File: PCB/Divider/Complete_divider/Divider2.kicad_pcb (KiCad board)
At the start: 2 copper layers, 98 x 48 mm, 56 parts, among them J31 Electr., J58 Electr.

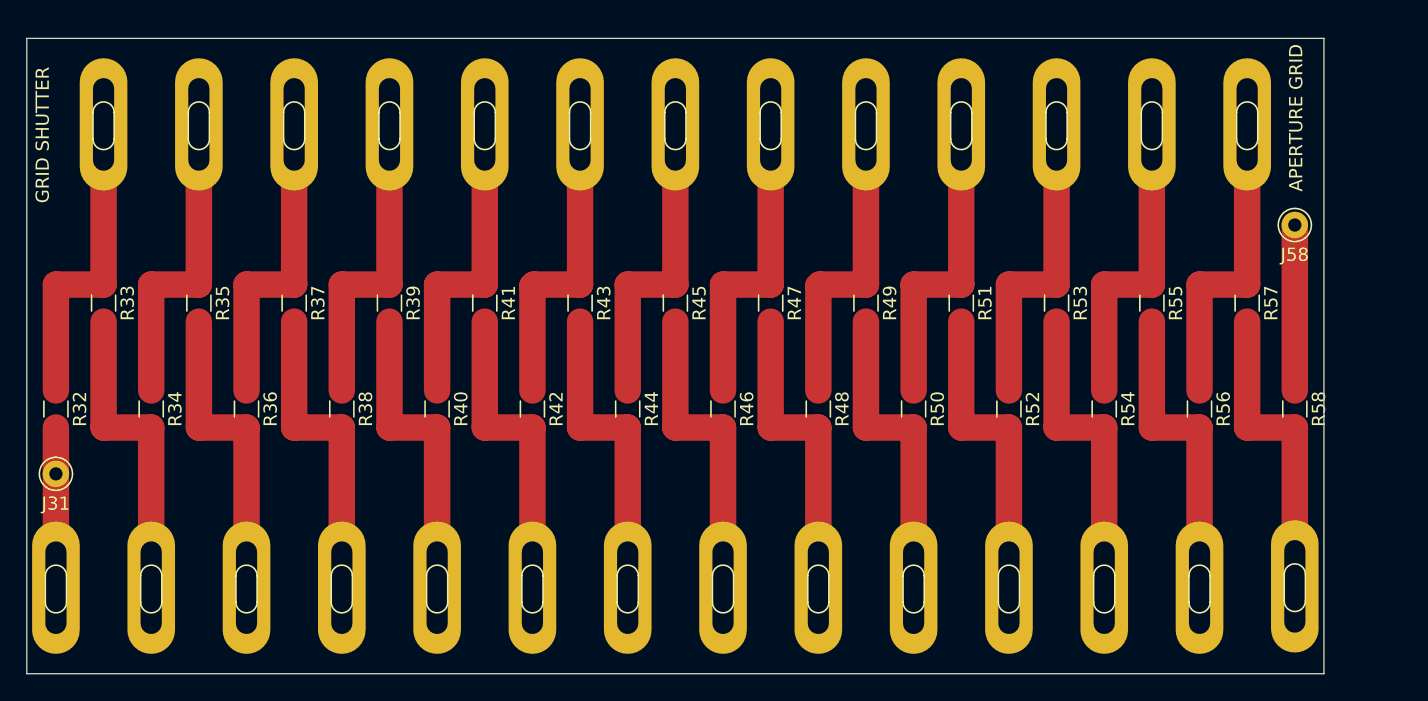
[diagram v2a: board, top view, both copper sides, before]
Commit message: Divider finished with test points
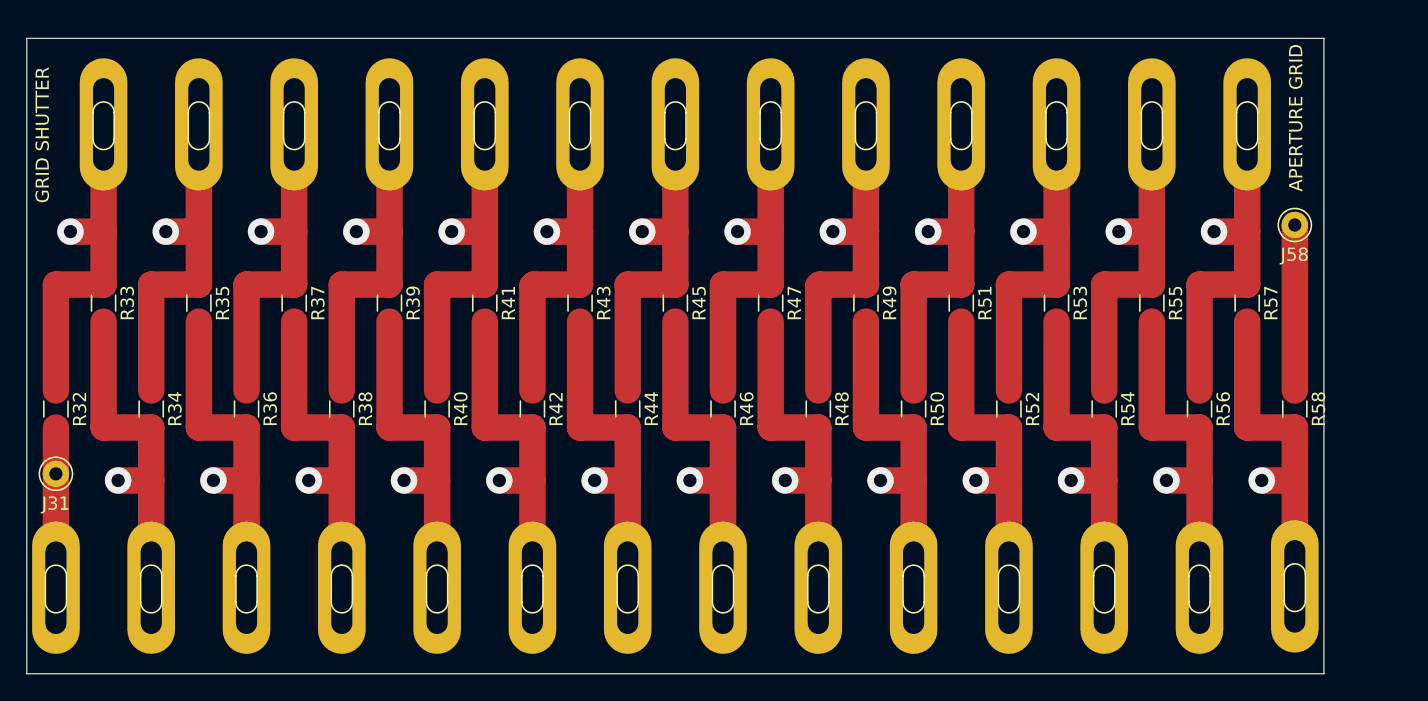
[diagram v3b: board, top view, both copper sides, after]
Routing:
- net Net-(E57-Pad1): track 23.6 -> 26.1 mm, vias 0 -> 1
- net Net-(E56-Pad1): track 23.7 -> 26.2 mm, vias 0 -> 1
- net Net-(E55-Pad1): track 23.7 -> 26.2 mm, vias 0 -> 1
- net Net-(E54-Pad1): track 23.7 -> 26.2 mm, vias 0 -> 1
- net Net-(E53-Pad1): track 23.7 -> 26.2 mm, vias 0 -> 1
- net Net-(E52-Pad1): track 23.7 -> 26.2 mm, vias 0 -> 1
- net Net-(E51-Pad1): track 23.7 -> 26.2 mm, vias 0 -> 1
- net Net-(E50-Pad1): track 23.7 -> 26.2 mm, vias 0 -> 1
- net Net-(E49-Pad1): track 23.7 -> 26.2 mm, vias 0 -> 1
- net Net-(E48-Pad1): track 23.6 -> 26.1 mm, vias 0 -> 1
- net Net-(E47-Pad1): track 23.7 -> 26.2 mm, vias 0 -> 1
- net Net-(E46-Pad1): track 23.7 -> 26.2 mm, vias 0 -> 1
- net Net-(E45-Pad1): track 23.7 -> 26.2 mm, vias 0 -> 1
- net Net-(E44-Pad1): track 23.7 -> 26.2 mm, vias 0 -> 1
- net Net-(E43-Pad1): track 23.7 -> 26.2 mm, vias 0 -> 1
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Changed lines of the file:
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@@
     (thickness 1.6)
     (drawings 16)
-    (tracks 83)
+    (tracks 162)
     (zones 0)
     (modules 56)
@@
     (via_min_size 0.4)
     (via_min_drill 0.3)
+    (user_via 2 1)
     (uvia_size 0.3)
     (uvia_drill 0.1)
@@
   (segment (start 99.6 109.2) (end 99.6 100.6) (width 2) (layer F.Cu) (net 2))
   (segment (start 99.6 100.6) (end 99.6 97.1) (width 2) (layer F.Cu) (net 2))
-  (segment (start 103.2 74.2) (end 103.2 86.3) (width 2) (layer F.Cu) (net 3))
   (segment (start 99.6 94.3) (end 99.6 86.3) (width 2) (layer F.Cu) (net 3))
   (segment (start 99.6 86.3) (end 103.2 86.3) (width 2) (layer F.Cu) (net 3))
+  (segment (start 103.2 74.2) (end 103.2 82.3) (width 2) (layer F.Cu) (net 3))
+  (segment (start 103.2 82.3) (end 100.7 82.3) (width 2) (layer F.Cu) (net 3))
+  (segment (start 103.2 82.3) (end 103.2 86.3) (width 2) (layer F.Cu) (net 3))
+  (segment (start 100.7 82.3) (end 100.7 82.3) (width 2) (layer F.Cu) (net 3))
+  (via (at 100.7 82.3) (size 2) (drill 1) (layers F.Cu B.Cu) (net 3))
+  (segment (start 107.9 82.3) (end 107.9 82.3) (width 2) (layer F.Cu) (net 5))
+  (segment (start 115.1 82.3) (end 115.1 82.3) (width 2) (layer F.Cu) (net 7))
+  (segment (start 122.3 82.3) (end 122.3 82.3) (width 2) (layer F.Cu) (net 9))
+  (segment (start 129.5 82.3) (end 129.5 82.3) (width 2) (layer F.Cu) (net 11))
+  (segment (start 136.7 82.3) (end 136.7 82.3) (width 2) (layer F.Cu) (net 13))
+  (segment (start 143.9 82.3) (end 143.9 82.3) (width 2) (layer F.Cu) (net 15))
+  (segment (start 151.1 82.3) (end 151.1 82.3) (width 2) (layer F.Cu) (net 17))
+  (segment (start 158.3 82.3) (end 158.3 82.3) (width 2) (layer F.Cu) (net 19))
+  (segment (start 165.5 82.3) (end 165.5 82.3) (width 2) (layer F.Cu) (net 21))
+  (segment (start 172.7 82.3) (end 172.7 82.3) (width 2) (layer F.Cu) (net 23))
+  (segment (start 179.9 82.3) (end 179.9 82.3) (width 2) (layer F.Cu) (net 25))
+  (segment (start 187.1 82.3) (end 187.1 82.3) (width 2) (layer F.Cu) (net 27))
+  (segment (start 104.3 101.1) (end 104.3 101.1) (width 2) (layer F.Cu) (net 4))
+  (segment (start 111.5 101.1) (end 111.5 101.1) (width 2) (layer F.Cu) (net 6))
+  (segment (start 118.7 101.1) (end 118.7 101.1) (width 2) (layer F.Cu) (net 8))
+  (segment (start 125.9 101.1) (end 125.9 101.1) (width 2) (layer F.Cu) (net 10))
+  (segment (start 133.1 101.1) (end 133.1 101.1) (width 2) (layer F.Cu) (net 12))
+  (segment (start 140.3 101.1) (end 140.3 101.1) (width 2) (layer F.Cu) (net 14))
+  (segment (start 147.5 101.1) (end 147.5 101.1) (width 2) (layer F.Cu) (net 16))
+  (segment (start 154.7 101.1) (end 154.7 101.1) (width 2) (layer F.Cu) (net 18))
+  (segment (start 161.9 101.1) (end 161.9 101.1) (width 2) (layer F.Cu) (net 20))
+  (segment (start 169.1 101.1) (end 169.1 101.1) (width 2) (layer F.Cu) (net 22))
+  (segment (start 176.3 101.1) (end 176.3 101.1) (width 2) (layer F.Cu) (net 24))
+  (segment (start 183.5 101.1) (end 183.5 101.1) (width 2) (layer F.Cu) (net 26))
+  (segment (start 190.7 101.1) (end 190.7 101.1) (width 2) (layer F.Cu) (net 28))
+  (via (at 107.9 82.3) (size 2) (drill 1) (layers F.Cu B.Cu) (net 5))
+  (via (at 115.1 82.3) (size 2) (drill 1) (layers F.Cu B.Cu) (net 7))
+  (via (at 122.3 82.3) (size 2) (drill 1) (layers F.Cu B.Cu) (net 9))
+  (via (at 129.5 82.3) (size 2) (drill 1) (layers F.Cu B.Cu) (net 11))
+  (via (at 136.7 82.3) (size 2) (drill 1) (layers F.Cu B.Cu) (net 13))
+  (via (at 143.9 82.3) (size 2) (drill 1) (layers F.Cu B.Cu) (net 15))
+  (via (at 151.1 82.3) (size 2) (drill 1) (layers F.Cu B.Cu) (net 17))
+  (via (at 158.3 82.3) (size 2) (drill 1) (layers F.Cu B.Cu) (net 19))
+  (via (at 165.5 82.3) (size 2) (drill 1) (layers F.Cu B.Cu) (net 21))
+  (via (at 172.7 82.3) (size 2) (drill 1) (layers F.Cu B.Cu) (net 23))
+  (via (at 179.9 82.3) (size 2) (drill 1) (layers F.Cu B.Cu) (net 25))
+  (via (at 187.1 82.3) (size 2) (drill 1) (layers F.Cu B.Cu) (net 27))
+  (via (at 104.3 101.1) (size 2) (drill 1) (layers F.Cu B.Cu) (net 4))
+  (via (at 111.5 101.1) (size 2) (drill 1) (layers F.Cu B.Cu) (net 6))
+  (via (at 118.7 101.1) (size 2) (drill 1) (layers F.Cu B.Cu) (net 8))
+  (via (at 125.9 101.1) (size 2) (drill 1) (layers F.Cu B.Cu) (net 10))
+  (via (at 133.1 101.1) (size 2) (drill 1) (layers F.Cu B.Cu) (net 12))
+  (via (at 140.3 101.1) (size 2) (drill 1) (layers F.Cu B.Cu) (net 14))
+  (via (at 147.5 101.1) (size 2) (drill 1) (layers F.Cu B.Cu) (net 16))
+  (via (at 154.7 101.1) (size 2) (drill 1) (layers F.Cu B.Cu) (net 18))
+  (via (at 161.9 101.1) (size 2) (drill 1) (layers F.Cu B.Cu) (net 20))
+  (via (at 169.1 101.1) (size 2) (drill 1) (layers F.Cu B.Cu) (net 22))
+  (via (at 176.3 101.1) (size 2) (drill 1) (layers F.Cu B.Cu) (net 24))
+  (via (at 183.5 101.1) (size 2) (drill 1) (layers F.Cu B.Cu) (net 26))
+  (via (at 190.7 101.1) (size 2) (drill 1) (layers F.Cu B.Cu) (net 28))
+  (segment (start 110.4 82.3) (end 107.9 82.3) (width 2) (layer F.Cu) (net 5))
+  (segment (start 117.6 82.3) (end 115.1 82.3) (width 2) (layer F.Cu) (net 7))
+  (segment (start 124.8 82.3) (end 122.3 82.3) (width 2) (layer F.Cu) (net 9))
+  (segment (start 132 82.3) (end 129.5 82.3) (width 2) (layer F.Cu) (net 11))
+  (segment (start 139.2 82.3) (end 136.7 82.3) (width 2) (layer F.Cu) (net 13))
+  (segment (start 146.4 82.3) (end 143.9 82.3) (width 2) (layer F.Cu) (net 15))
+  (segment (start 153.6 82.3) (end 151.1 82.3) (width 2) (layer F.Cu) (net 17))
+  (segment (start 160.8 82.3) (end 158.3 82.3) (width 2) (layer F.Cu) (net 19))
+  (segment (start 168 82.3) (end 165.5 82.3) (width 2) (layer F.Cu) (net 21))
+  (segment (start 175.2 82.3) (end 172.7 82.3) (width 2) (layer F.Cu) (net 23))
+  (segment (start 182.4 82.3) (end 179.9 82.3) (width 2) (layer F.Cu) (net 25))
+  (segment (start 189.6 82.3) (end 187.1 82.3) (width 2) (layer F.Cu) (net 27))
+  (segment (start 106.8 101.1) (end 104.3 101.1) (width 2) (layer F.Cu) (net 4))
+  (segment (start 114 101.1) (end 111.5 101.1) (width 2) (layer F.Cu) (net 6))
+  (segment (start 121.2 101.1) (end 118.7 101.1) (width 2) (layer F.Cu) (net 8))
+  (segment (start 128.4 101.1) (end 125.9 101.1) (width 2) (layer F.Cu) (net 10))
+  (segment (start 135.6 101.1) (end 133.1 101.1) (width 2) (layer F.Cu) (net 12))
+  (segment (start 142.8 101.1) (end 140.3 101.1) (width 2) (layer F.Cu) (net 14))
+  (segment (start 150 101.1) (end 147.5 101.1) (width 2) (layer F.Cu) (net 16))
+  (segment (start 157.2 101.1) (end 154.7 101.1) (width 2) (layer F.Cu) (net 18))
+  (segment (start 164.4 101.1) (end 161.9 101.1) (width 2) (layer F.Cu) (net 20))
+  (segment (start 171.6 101.1) (end 169.1 101.1) (width 2) (layer F.Cu) (net 22))
+  (segment (start 178.8 101.1) (end 176.3 101.1) (width 2) (layer F.Cu) (net 24))
+  (segment (start 186 101.1) (end 183.5 101.1) (width 2) (layer F.Cu) (net 26))
+  (segment (start 193.2 101.1) (end 190.7 101.1) (width 2) (layer F.Cu) (net 28))
   (segment (start 103.2 89.1) (end 103.2 97.1) (width 2) (layer F.Cu) (net 4))
   (segment (start 103.2 97.1) (end 106.8 97.1) (width 2) (layer F.Cu) (net 4))

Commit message: Most parts completed
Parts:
- renumbered J58 to E58, R32 to R31, R33 to R32, R34 to R33, R35 to R34, R36 to R35, R37 to R36, R38 to R37, R39 to R38, R40 to R39, R41 to R40, R42 to R41, R43 to R42, R44 to R43, R45 to R44, R46 to R45, R47 to R46, R48 to R47, R49 to R48, R50 to R49, R51 to R50, R52 to R51, R53 to R52, R54 to R53, R55 to R54, R56 to R55, R57 to R56, R58 to R57

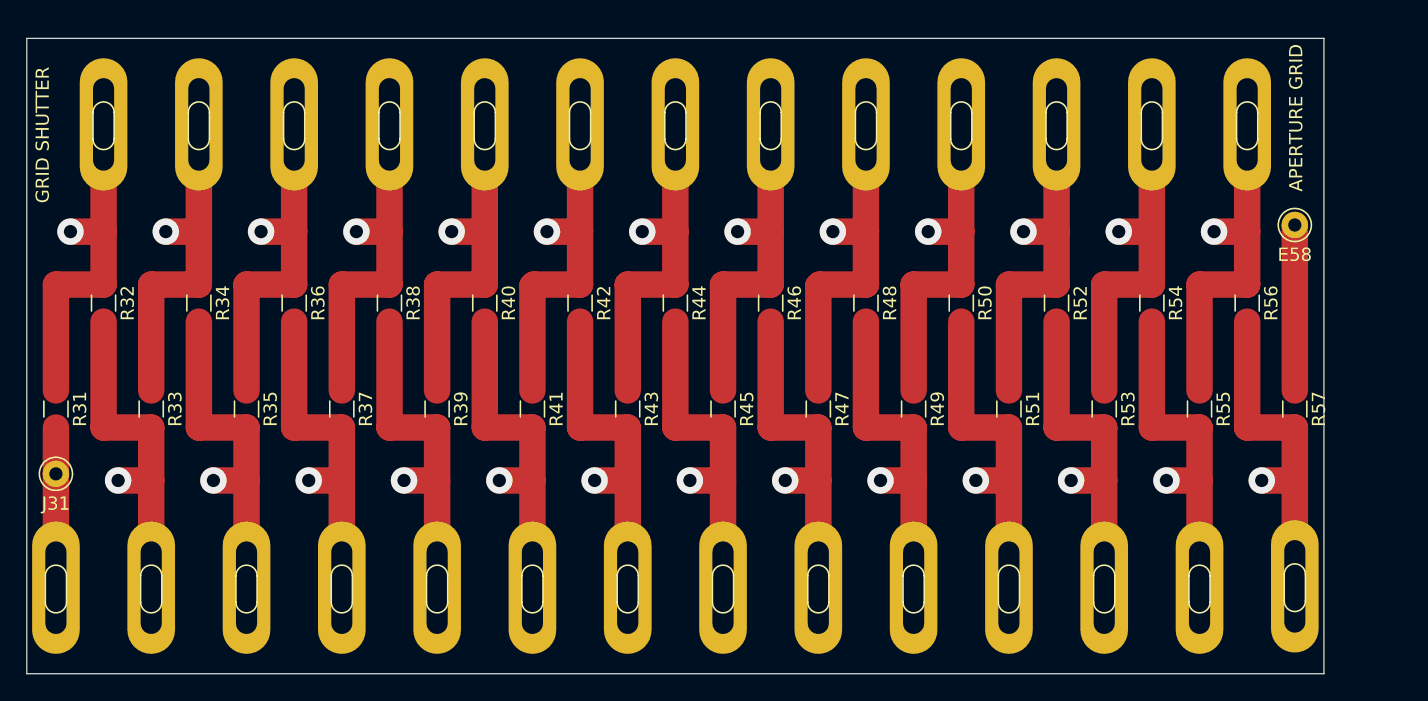
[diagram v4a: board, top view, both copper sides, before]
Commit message: Updates of dividers 1 & 2
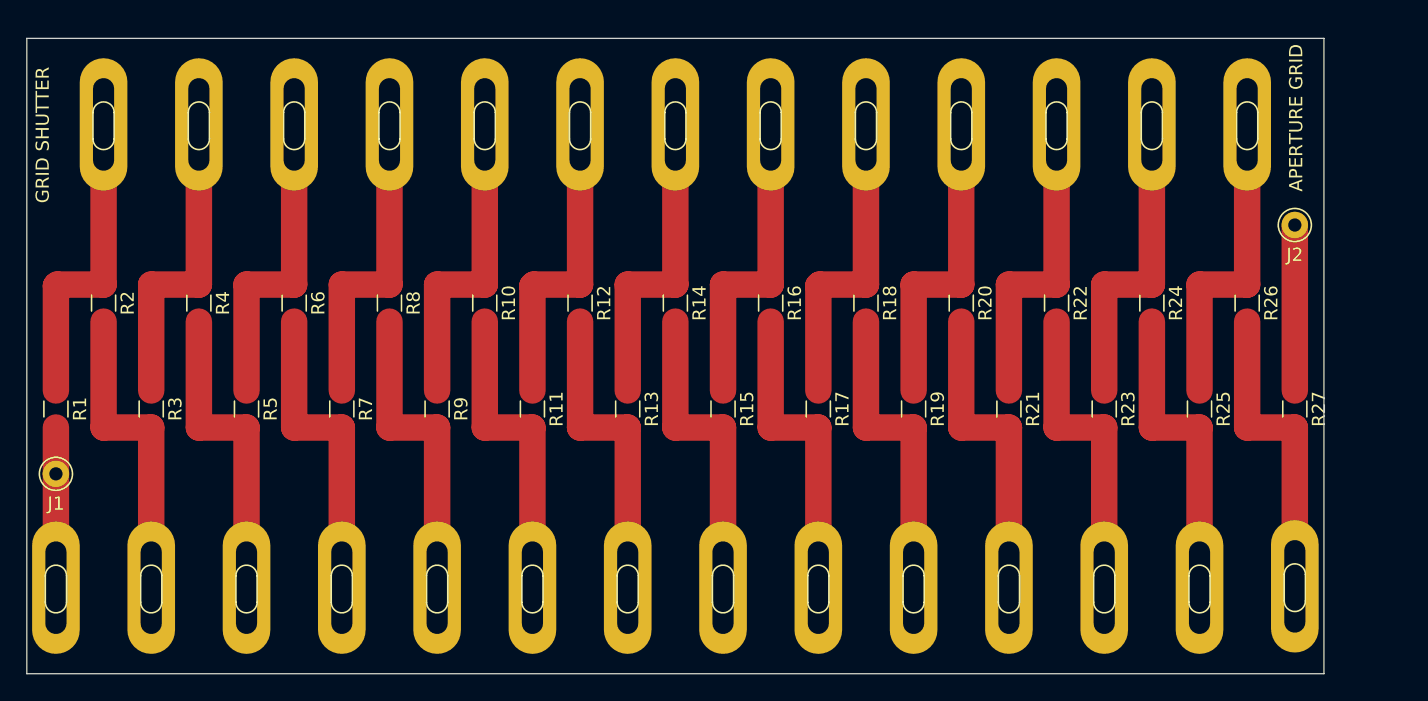
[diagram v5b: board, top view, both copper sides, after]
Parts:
- J1: renamed from J31; value Electr. -> Pwr In
- J2: renamed from E58; value Electr. -> PWR out
- renumbered E31 to E1, E40 to E10, E41 to E11, E42 to E12, E43 to E13, E44 to E14, E45 to E15, E46 to E16, E47 to E17, E48 to E18, E49 to E19, E32 to E2, E50 to E20, E51 to E21, E52 to E22, E53 to E23, E54 to E24, E55 to E25, E56 to E26, E57 to E27, E33 to E3, E34 to E4, E35 to E5, E36 to E6, E37 to E7, E38 to E8, E39 to E9, R31 to R1, R40 to R10, R41 to R11, R42 to R12, R43 to R13, R44 to R14, R45 to R15, R46 to R16, R47 to R17, R48 to R18, R49 to R19, R32 to R2, R50 to R20, R51 to R21, R52 to R22, R53 to R23, R54 to R24, R55 to R25, R56 to R26, R57 to R27, R33 to R3, R34 to R4, R35 to R5, R36 to R6, R37 to R7, R38 to R8, R39 to R9
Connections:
- net DRIFTTUBE renamed DRIFT_TUBE
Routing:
- net Net-(E2-Pad1): track 26.2 -> 23.6 mm, vias 1 -> 0
- net Net-(E9-Pad1): track 26.2 -> 23.7 mm, vias 1 -> 0
- net Net-(E8-Pad1): track 26.2 -> 23.7 mm, vias 1 -> 0
- net Net-(E7-Pad1): track 26.2 -> 23.7 mm, vias 1 -> 0
- net Net-(E6-Pad1): track 26.2 -> 23.7 mm, vias 1 -> 0
- net Net-(E5-Pad1): track 26.2 -> 23.7 mm, vias 1 -> 0
- net Net-(E4-Pad1): track 26.2 -> 23.7 mm, vias 1 -> 0
- net Net-(E3-Pad1): track 26.2 -> 23.7 mm, vias 1 -> 0
- net Net-(E27-Pad1): track 26.1 -> 23.6 mm, vias 1 -> 0
- net Net-(E26-Pad1): track 26.2 -> 23.7 mm, vias 1 -> 0
- net Net-(E25-Pad1): track 26.2 -> 23.7 mm, vias 1 -> 0
- net Net-(E24-Pad1): track 26.2 -> 23.7 mm, vias 1 -> 0
- net Net-(E23-Pad1): track 26.2 -> 23.7 mm, vias 1 -> 0
- net Net-(E22-Pad1): track 26.2 -> 23.7 mm, vias 1 -> 0
- net Net-(E21-Pad1): track 26.2 -> 23.7 mm, vias 1 -> 0
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
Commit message: Update
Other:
- board size 98 x 48 mm -> 97.6 x 48 mm
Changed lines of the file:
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@@
     (38 B.Mask user)
     (39 F.Mask user)
-    (40 Dwgs.User user hide)
+    (40 Dwgs.User user)
     (41 Cmts.User user)
     (42 Eco1.User user)
@@
   )
   (setup
-    (last_trace_width 2)
+    (last_trace_width 0.25)
     (user_trace_width 2)
     (trace_clearance 0.2)
@@
     (mod_text_size 1 1)
     (mod_text_width 0.15)
-    (pad_size 3 10)
+    (pad_size 3.6 10)
     (pad_drill 1.6)
     (pad_to_mask_clearance 0.051)
@@
     (pcbplotparams
       (layerselection 0x010fc_ffffffff)
-      (usegerberextensions false)
+      (usegerberextensions true)
       (usegerberattributes false)
       (usegerberadvancedattributes false)
@@
       (outputformat 1)
       (mirror false)
-      (drillshape 1)
+      (drillshape 0)
       (scaleselection 1)
-      (outputdirectory ""))
+      (outputdirectory "../../../../../../Desktop/GERBER_IMS_1/Divider2/"))
   )
   (net 0 "")
@@
     (fp_line (start 0.8 -1) (end 0.8 1) (layer F.SilkS) (width 0.12))
     (fp_line (start -0.8 1) (end -0.8 -1) (layer F.SilkS) (width 0.12))
-    (pad 1 thru_hole oval (at 0 -0.1) (size 3.6 10) (drill oval 1.6 7) (layers *.Cu *.Mask)
+    (pad 1 thru_hole oval (at 0 -0.1) (size 3.4 10) (drill oval 1.6 7) (layers *.Cu *.Mask)
       (net 2 DRIFT_TUBE))
   )
@@
   (gr_line (start 98.3 95.7) (end 198.9 95.7) (layer Dwgs.User) (width 0.15))
   (gr_line (start 95.6 87.7) (end 196.2 87.7) (layer Dwgs.User) (width 0.15))
-  (gr_line (start 195.4 67.7) (end 97.4 67.7) (layer Edge.Cuts) (width 0.05))
+  (gr_line (start 195.4 67.7) (end 97.8 67.7) (layer Edge.Cuts) (width 0.05))
   (dimension 48 (width 0.15) (layer Dwgs.User)
     (gr_text "48,000 mm" (at 89.1 91.7 90) (layer Dwgs.User)
@@
     (arrow2b (pts (xy 90.4 115.7) (xy 89.813579 114.573496)))
   )
-  (dimension 98 (width 0.15) (layer Dwgs.User)
-    (gr_text "98,000 mm" (at 146.4 62.9) (layer Dwgs.User)
-      (effects (font (size 1 1) (thickness 0.15)))
-    )
-    (feature1 (pts (xy 195.4 67.2) (xy 195.4 63.613579)))
-    (feature2 (pts (xy 97.4 67.2) (xy 97.4 63.613579)))
-    (crossbar (pts (xy 97.4 64.2) (xy 195.4 64.2)))
-    (arrow1a (pts (xy 195.4 64.2) (xy 194.273496 64.786421)))
-    (arrow1b (pts (xy 195.4 64.2) (xy 194.273496 63.613579)))
-    (arrow2a (pts (xy 97.4 64.2) (xy 98.526504 64.786421)))
-    (arrow2b (pts (xy 97.4 64.2) (xy 98.526504 63.613579)))
-  )
-  (gr_line (start 97.4 67.7) (end 97.4 115.7) (layer Edge.Cuts) (width 0.05))
-  (gr_line (start 97.4 115.7) (end 195.4 115.7) (layer Edge.Cuts) (width 0.05))
+  (dimension 97.6 (width 0.15) (layer Dwgs.User)
+    (gr_text "97,600 mm" (at 146.6 62.8) (layer Dwgs.User)
+      (effects (font (size 1 1) (thickness 0.15)))
+    )
+    (feature1 (pts (xy 195.4 67.2) (xy 195.4 63.513579)))
+    (feature2 (pts (xy 97.8 67.2) (xy 97.8 63.513579)))
+    (crossbar (pts (xy 97.8 64.1) (xy 195.4 64.1)))
+    (arrow1a (pts (xy 195.4 64.1) (xy 194.273496 64.686421)))
+    (arrow1b (pts (xy 195.4 64.1) (xy 194.273496 63.513579)))
+    (arrow2a (pts (xy 97.8 64.1) (xy 98.926504 64.686421)))
+    (arrow2b (pts (xy 97.8 64.1) (xy 98.926504 63.513579)))
+  )
+  (gr_line (start 97.8 67.7) (end 97.8 115.7) (layer Edge.Cuts) (width 0.05))
+  (gr_line (start 97.8 115.7) (end 195.4 115.7) (layer Edge.Cuts) (width 0.05))
   (gr_line (start 195.4 115.7) (end 195.4 67.7) (layer Edge.Cuts) (width 0.05))
   (gr_line (start 94.6 109.2) (end 201 109.2) (layer Dwgs.User) (width 0.15))
